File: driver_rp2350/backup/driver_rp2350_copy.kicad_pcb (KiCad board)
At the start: 6 copper layers, 45 x 45 mm, 463 parts, among them J1 Conn_01x04, J2 Conn_01x05, J3 Conn_01x05, J4 Conn_01x05, J5 Conn_01x05, SW1 SW_Push, SW2 SW_Push, U1 APS6404L-3SQR, U10 UCC27517, U11 UCC27517, U12 UCC27517, U13 UCC27517, U14 UCC27517, U15 UCC27517, U16 UCC27517, U17 UCC27517, U18 UCC27517, U19 UCC27517, U2 RP2354B_80QFN, U20 UCC27517, U21 UCC27517, U22 UCC27517, U23 UCC27517, U24 UCC27517, U25 UCC27517, U26 UCC27517, U27 UCC27517, U28 UCC27517, U29 UCC27517, U3 UCC27517, U30 UCC27517, U31 UCC27517, U32 UCC27517, U33 UCC27517, U34 UCC27517, U35 UCC27517, U36 UCC27517, U37 UCC27517, U38 UCC27517, U39 AP2112K-3.3, U4 UCC27517, U5 UCC27517, U6 UCC27517, U7 UCC27517, U8 UCC27517, U9 UCC27517, Y1 ABM8-272-T3

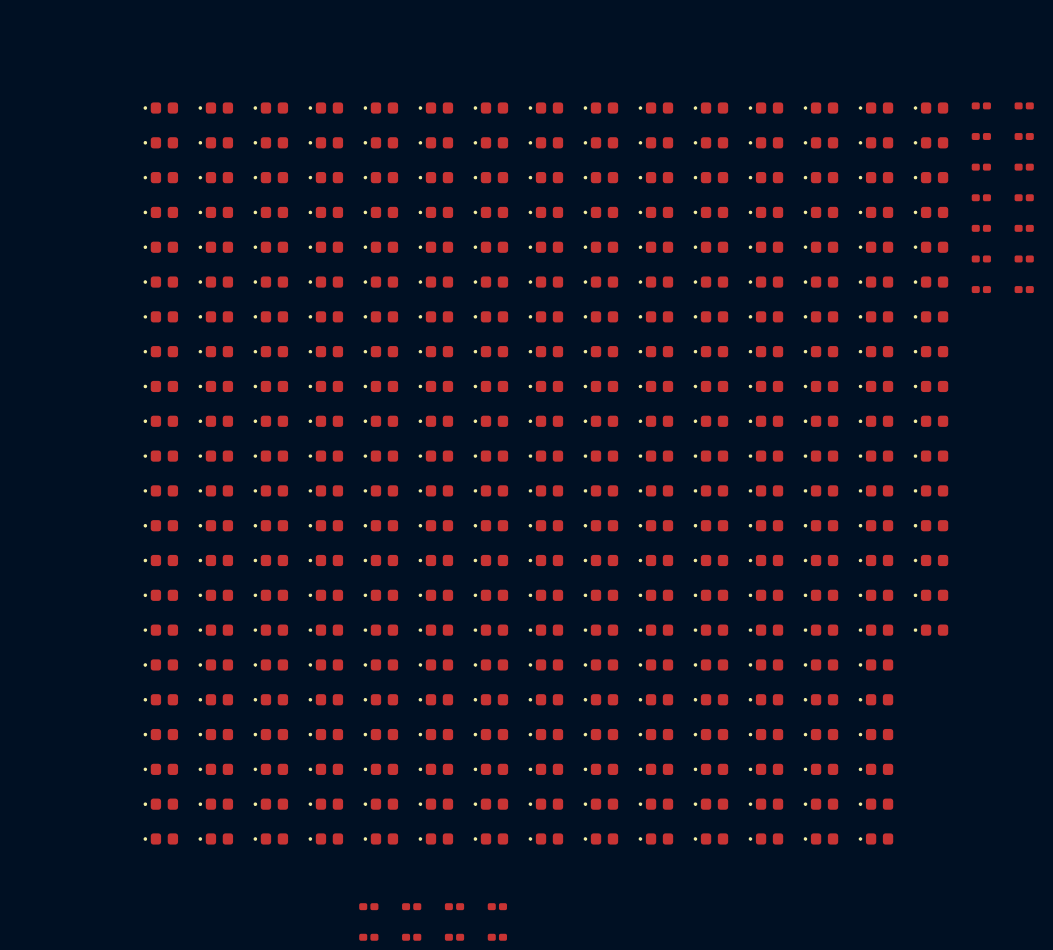
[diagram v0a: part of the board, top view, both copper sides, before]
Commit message: Worked on multi-color led layout.
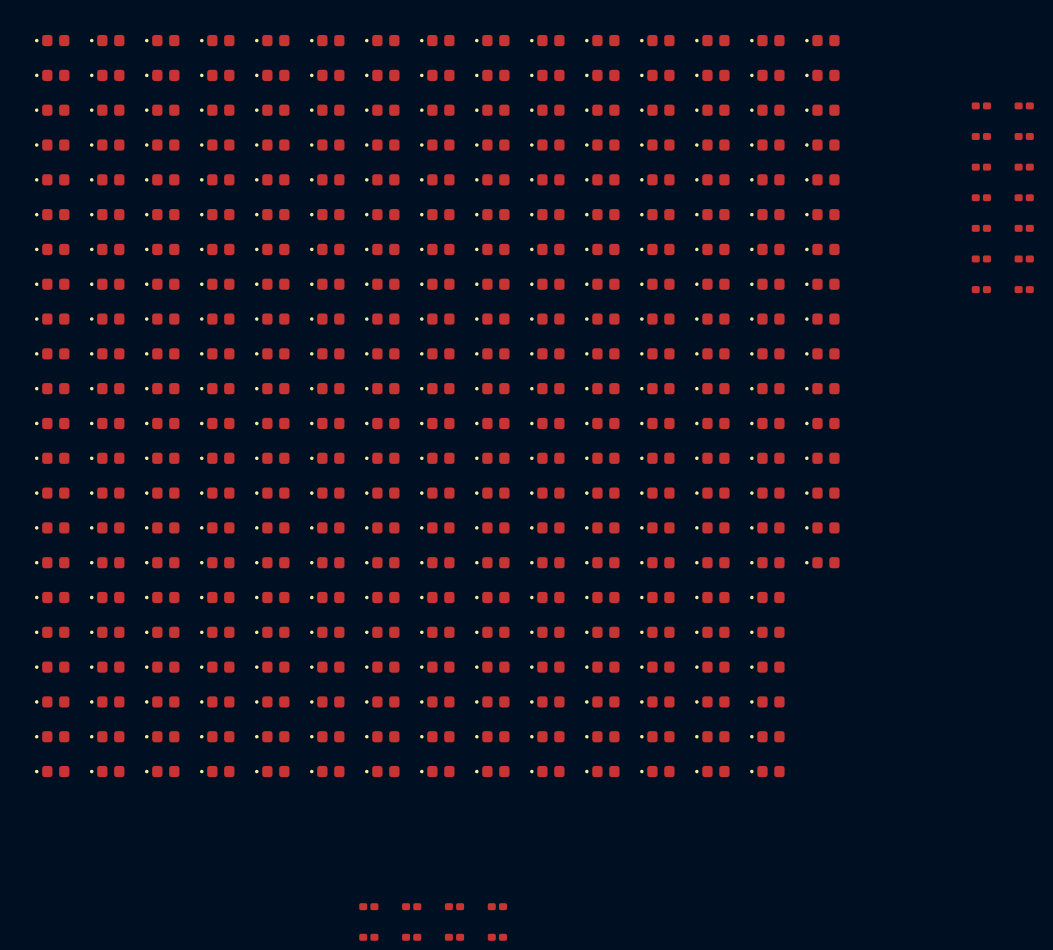
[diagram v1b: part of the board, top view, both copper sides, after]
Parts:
- removed D_0A1, D_0B1, D_0C1, D_0D1, D_0E1, D_0F1, D_0G1, D_0H1, D_1, D_10, D_100, D_11, D_12, D_13, D_14, D_15, D_16, D_17, D_18, D_19, D_1A1, D_1B1, D_1C1, D_1D1, D_1E1, D_1F1, D_1G1, D_1H1, D_2, D_20, D_21, D_22, D_23, D_24, D_25, D_26, D_27, D_28, D_29, D_2A1, D_2B1, D_2C1, D_2D1, D_2E1, D_2F1, D_2G1, D_2H1, D_3, D_30, D_31, D_32, D_33, D_34, D_35, D_36, D_37, D_38, D_39, D_3A1, D_3B1, D_3C1, D_3D1, D_3E1, D_3F1, D_3G1, D_3H1, D_4, D_40, D_41, D_42, D_43, D_44, D_45, D_46, D_47, D_48, D_49, D_4A1, D_4B1, D_4C1, D_4D1, D_4E1, D_4F1, D_4G1, D_4H1, D_5, D_50, D_51, D_52, D_53, D_54, D_55, D_56, D_57, D_58, D_59, D_5A1, D_5B1, D_5C1, D_5D1, D_5E1, D_5F1, D_5G1, D_5H1, D_6, D_60, D_61, D_62, D_63, D_64, D_65, D_66, D_67, D_68, D_69, D_6A1, D_6B1, D_6C1, D_6D1, D_6E1, D_6F1, D_6G1, D_6H1, D_7, D_70, D_71, D_72, D_73, D_74, D_75, D_76, D_77, D_78, D_79, D_7A1, D_7B1, D_7C1, D_7D1, D_7E1, D_7F1, D_7G1, D_7H1, D_8, D_80, D_81, D_82, D_83, D_84, D_85, D_86, D_87, D_88, D_89, D_8A1, D_8B1, D_8C1, D_8D1, D_8E1, D_8F1, D_8G1, D_8H1, D_9, D_90, D_91, D_92, D_93, D_94, D_95, D_96, D_97, D_98, D_99, D_9A1, D_9B1, D_9C1, D_9D1, D_9E1, D_9F1, D_9G1, D_9H1, D_A1, D_A10, D_A2, D_A3, D_A4, D_A5, D_A6, D_A7, D_A8, D_A9, D_AA1, D_AB1, D_AC1, D_AD1, D_AE1, D_AF1, D_AG1, D_AH1, D_B1, D_B10, D_B2, D_B3, D_B4, D_B5, D_B6, D_B7, D_B8, D_B9, D_BA1, D_BB1, D_BC1, D_BD1, D_BE1, D_BF1, D_BG1, D_BH1, D_C1, D_C10, D_C2, D_C3, D_C4, D_C5, D_C6, D_C7, D_C8, D_C9, D_CA1, D_CB1, D_CC1, D_CD1, D_CE1, D_CF1, D_CG1, D_CH1, D_D1, D_D10, D_D2, D_D3, D_D4, D_D5, D_D6, D_D7, D_D8, D_D9, D_DA1, D_DB1, D_DC1, D_DD1, D_DE1, D_DF1, D_DG1, D_DH1, D_E1, D_E10, D_E2, D_E3, D_E4, D_E5, D_E6, D_E7, D_E8, D_E9, D_EA1, D_EB1, D_EC1, D_ED1, D_EE1, D_EF1, D_EG1, D_EH1, D_F1, D_F10, D_F2, D_F3, D_F4, D_F5, D_F6, D_F7, D_F8, D_F9, D_FA1, D_FB1, D_FC1, D_FD1, D_FE1, D_FF1, D_FG1, D_FH1, D_G1, D_G10, D_G2, D_G3, D_G4, D_G5, D_G6, D_G7, D_G8, D_G9, D_GA1, D_GB1, D_GC1, D_GD1, D_GE1, D_GF1, D_GG1, D_GH1, D_H1, D_H10, D_H2, D_H3, D_H4, D_H5, D_H6, D_H7, D_H8, D_H9, D_HA1, D_HB1, D_HC1, D_HD1, D_HE1, D_HF1, D_HG1, D_HH1: LED, panel_custom:LED_0402_1005Metric
- added D1: LED, panel_custom:LED_0402_1005Metric, F.Cu at (-66.4, -11.2)
- added D10: LED, panel_custom:LED_0402_1005Metric, F.Cu at (-66.4, 6.72)
- added D100: LED, panel_custom:LED_0402_1005Metric, F.Cu at (-53.8, 10.7)
- added D101: LED, panel_custom:LED_0402_1005Metric, F.Cu at (-53.8, 12.7)
- added D102: LED, panel_custom:LED_0402_1005Metric, F.Cu at (-53.8, 14.7)
- added D103: LED, panel_custom:LED_0402_1005Metric, F.Cu at (-53.8, 16.7)
- added D104: LED, panel_custom:LED_0402_1005Metric, F.Cu at (-53.8, 18.7)
- added D105: LED, panel_custom:LED_0402_1005Metric, F.Cu at (-53.8, 20.6)
- added D106: LED, panel_custom:LED_0402_1005Metric, F.Cu at (-53.8, 22.6)
- added D107: LED, panel_custom:LED_0402_1005Metric, F.Cu at (-53.8, 24.6)
- added D108: LED, panel_custom:LED_0402_1005Metric, F.Cu at (-53.8, 26.6)
- added D109: LED, panel_custom:LED_0402_1005Metric, F.Cu at (-53.8, 28.6)
- added D11: LED, panel_custom:LED_0402_1005Metric, F.Cu at (-66.4, 8.71)
- added D110: LED, panel_custom:LED_0402_1005Metric, F.Cu at (-53.8, 30.6)
- added D111: LED, panel_custom:LED_0402_1005Metric, F.Cu at (-50.6, -11.2)
- added D112: LED, panel_custom:LED_0402_1005Metric, F.Cu at (-50.6, -9.20)
- added D113: LED, panel_custom:LED_0402_1005Metric, F.Cu at (-50.6, -7.21)
- added D114: LED, panel_custom:LED_0402_1005Metric, F.Cu at (-50.6, -5.22)
- added D115: LED, panel_custom:LED_0402_1005Metric, F.Cu at (-50.6, -3.23)
- added D116: LED, panel_custom:LED_0402_1005Metric, F.Cu at (-50.6, -1.24)
- added D117: LED, panel_custom:LED_0402_1005Metric, F.Cu at (-50.6, 0.75)
- added D118: LED, panel_custom:LED_0402_1005Metric, F.Cu at (-50.6, 2.74)
- added D119: LED, panel_custom:LED_0402_1005Metric, F.Cu at (-50.6, 4.73)
- added D12: LED, panel_custom:LED_0402_1005Metric, F.Cu at (-66.4, 10.7)
- added D120: LED, panel_custom:LED_0402_1005Metric, F.Cu at (-50.6, 6.72)
- added D121: LED, panel_custom:LED_0402_1005Metric, F.Cu at (-50.6, 8.71)
- added D122: LED, panel_custom:LED_0402_1005Metric, F.Cu at (-50.6, 10.7)
- added D123: LED, panel_custom:LED_0402_1005Metric, F.Cu at (-50.6, 12.7)
- added D124: LED, panel_custom:LED_0402_1005Metric, F.Cu at (-50.6, 14.7)
- added D125: LED, panel_custom:LED_0402_1005Metric, F.Cu at (-50.6, 16.7)
- added D126: LED, panel_custom:LED_0402_1005Metric, F.Cu at (-50.6, 18.7)
- added D127: LED, panel_custom:LED_0402_1005Metric, F.Cu at (-50.6, 20.6)
- added D128: LED, panel_custom:LED_0402_1005Metric, F.Cu at (-50.6, 22.6)
- added D129: LED, panel_custom:LED_0402_1005Metric, F.Cu at (-50.6, 24.6)
- added D13: LED, panel_custom:LED_0402_1005Metric, F.Cu at (-66.4, 12.7)
- added D130: LED, panel_custom:LED_0402_1005Metric, F.Cu at (-50.6, 26.6)
- added D131: LED, panel_custom:LED_0402_1005Metric, F.Cu at (-50.6, 28.6)
- added D132: LED, panel_custom:LED_0402_1005Metric, F.Cu at (-50.6, 30.6)
- added D133: LED, panel_custom:LED_0402_1005Metric, F.Cu at (-47.5, -11.2)
- added D134: LED, panel_custom:LED_0402_1005Metric, F.Cu at (-47.5, -9.20)
- added D135: LED, panel_custom:LED_0402_1005Metric, F.Cu at (-47.5, -7.21)
- added D136: LED, panel_custom:LED_0402_1005Metric, F.Cu at (-47.5, -5.22)
- added D137: LED, panel_custom:LED_0402_1005Metric, F.Cu at (-47.5, -3.23)
- added D138: LED, panel_custom:LED_0402_1005Metric, F.Cu at (-47.5, -1.24)
- added D139: LED, panel_custom:LED_0402_1005Metric, F.Cu at (-47.5, 0.75)
- added D14: LED, panel_custom:LED_0402_1005Metric, F.Cu at (-66.4, 14.7)
- added D140: LED, panel_custom:LED_0402_1005Metric, F.Cu at (-47.5, 2.74)
- added D141: LED, panel_custom:LED_0402_1005Metric, F.Cu at (-47.5, 4.73)
- added D142: LED, panel_custom:LED_0402_1005Metric, F.Cu at (-47.5, 6.72)
- added D143: LED, panel_custom:LED_0402_1005Metric, F.Cu at (-47.5, 8.71)
- added D144: LED, panel_custom:LED_0402_1005Metric, F.Cu at (-47.5, 10.7)
- added D145: LED, panel_custom:LED_0402_1005Metric, F.Cu at (-47.5, 12.7)
- added D146: LED, panel_custom:LED_0402_1005Metric, F.Cu at (-47.5, 14.7)
- added D147: LED, panel_custom:LED_0402_1005Metric, F.Cu at (-47.5, 16.7)
- added D148: LED, panel_custom:LED_0402_1005Metric, F.Cu at (-47.5, 18.7)
- added D149: LED, panel_custom:LED_0402_1005Metric, F.Cu at (-47.5, 20.6)
- added D15: LED, panel_custom:LED_0402_1005Metric, F.Cu at (-66.4, 16.7)
- added D150: LED, panel_custom:LED_0402_1005Metric, F.Cu at (-47.5, 22.6)
- added D151: LED, panel_custom:LED_0402_1005Metric, F.Cu at (-47.5, 24.6)
- added D152: LED, panel_custom:LED_0402_1005Metric, F.Cu at (-47.5, 26.6)
- added D153: LED, panel_custom:LED_0402_1005Metric, F.Cu at (-47.5, 28.6)
- added D154: LED, panel_custom:LED_0402_1005Metric, F.Cu at (-47.5, 30.6)
- added D155: LED, panel_custom:LED_0402_1005Metric, F.Cu at (-44.4, -11.2)
- added D156: LED, panel_custom:LED_0402_1005Metric, F.Cu at (-44.4, -9.20)
- added D157: LED, panel_custom:LED_0402_1005Metric, F.Cu at (-44.4, -7.21)
- added D158: LED, panel_custom:LED_0402_1005Metric, F.Cu at (-44.4, -5.22)
- added D159: LED, panel_custom:LED_0402_1005Metric, F.Cu at (-44.4, -3.23)
- added D16: LED, panel_custom:LED_0402_1005Metric, F.Cu at (-66.4, 18.7)
- added D160: LED, panel_custom:LED_0402_1005Metric, F.Cu at (-44.4, -1.24)
- added D161: LED, panel_custom:LED_0402_1005Metric, F.Cu at (-44.4, 0.75)
- added D162: LED, panel_custom:LED_0402_1005Metric, F.Cu at (-44.4, 2.74)
- added D163: LED, panel_custom:LED_0402_1005Metric, F.Cu at (-44.4, 4.73)
- added D164: LED, panel_custom:LED_0402_1005Metric, F.Cu at (-44.4, 6.72)
- added D165: LED, panel_custom:LED_0402_1005Metric, F.Cu at (-44.4, 8.71)
- added D166: LED, panel_custom:LED_0402_1005Metric, F.Cu at (-44.4, 10.7)
- added D167: LED, panel_custom:LED_0402_1005Metric, F.Cu at (-44.4, 12.7)
- added D168: LED, panel_custom:LED_0402_1005Metric, F.Cu at (-44.4, 14.7)
- added D169: LED, panel_custom:LED_0402_1005Metric, F.Cu at (-44.4, 16.7)
- added D17: LED, panel_custom:LED_0402_1005Metric, F.Cu at (-66.4, 20.6)
- added D170: LED, panel_custom:LED_0402_1005Metric, F.Cu at (-44.4, 18.7)
- added D171: LED, panel_custom:LED_0402_1005Metric, F.Cu at (-44.4, 20.6)
- added D172: LED, panel_custom:LED_0402_1005Metric, F.Cu at (-44.4, 22.6)
- added D173: LED, panel_custom:LED_0402_1005Metric, F.Cu at (-44.4, 24.6)
- added D174: LED, panel_custom:LED_0402_1005Metric, F.Cu at (-44.4, 26.6)
- added D175: LED, panel_custom:LED_0402_1005Metric, F.Cu at (-44.4, 28.6)
- added D176: LED, panel_custom:LED_0402_1005Metric, F.Cu at (-44.4, 30.6)
- added D177: LED, panel_custom:LED_0402_1005Metric, F.Cu at (-41.2, -11.2)
- added D178: LED, panel_custom:LED_0402_1005Metric, F.Cu at (-41.2, -9.20)
- added D179: LED, panel_custom:LED_0402_1005Metric, F.Cu at (-41.2, -7.21)
- added D18: LED, panel_custom:LED_0402_1005Metric, F.Cu at (-66.4, 22.6)
- added D180: LED, panel_custom:LED_0402_1005Metric, F.Cu at (-41.2, -5.22)
- added D181: LED, panel_custom:LED_0402_1005Metric, F.Cu at (-41.2, -3.23)
- added D182: LED, panel_custom:LED_0402_1005Metric, F.Cu at (-41.2, -1.24)
- added D183: LED, panel_custom:LED_0402_1005Metric, F.Cu at (-41.2, 0.75)
- added D184: LED, panel_custom:LED_0402_1005Metric, F.Cu at (-41.2, 2.74)
- added D185: LED, panel_custom:LED_0402_1005Metric, F.Cu at (-41.2, 4.73)
- added D186: LED, panel_custom:LED_0402_1005Metric, F.Cu at (-41.2, 6.72)
- added D187: LED, panel_custom:LED_0402_1005Metric, F.Cu at (-41.2, 8.71)
- added D188: LED, panel_custom:LED_0402_1005Metric, F.Cu at (-41.2, 10.7)
- added D189: LED, panel_custom:LED_0402_1005Metric, F.Cu at (-41.2, 12.7)
- added D19: LED, panel_custom:LED_0402_1005Metric, F.Cu at (-66.4, 24.6)
- added D190: LED, panel_custom:LED_0402_1005Metric, F.Cu at (-41.2, 14.7)
- added D191: LED, panel_custom:LED_0402_1005Metric, F.Cu at (-41.2, 16.7)
- added D192: LED, panel_custom:LED_0402_1005Metric, F.Cu at (-41.2, 18.7)
- added D193: LED, panel_custom:LED_0402_1005Metric, F.Cu at (-41.2, 20.6)
- added D194: LED, panel_custom:LED_0402_1005Metric, F.Cu at (-41.2, 22.6)
- added D195: LED, panel_custom:LED_0402_1005Metric, F.Cu at (-41.2, 24.6)
- added D196: LED, panel_custom:LED_0402_1005Metric, F.Cu at (-41.2, 26.6)
- added D197: LED, panel_custom:LED_0402_1005Metric, F.Cu at (-41.2, 28.6)
- added D198: LED, panel_custom:LED_0402_1005Metric, F.Cu at (-41.2, 30.6)
- added D199: LED, panel_custom:LED_0402_1005Metric, F.Cu at (-38.1, -11.2)
- added D2: LED, panel_custom:LED_0402_1005Metric, F.Cu at (-66.4, -9.20)
- added D20: LED, panel_custom:LED_0402_1005Metric, F.Cu at (-66.4, 26.6)
- added D200: LED, panel_custom:LED_0402_1005Metric, F.Cu at (-38.1, -9.20)
- added D201: LED, panel_custom:LED_0402_1005Metric, F.Cu at (-38.1, -7.21)
- added D202: LED, panel_custom:LED_0402_1005Metric, F.Cu at (-38.1, -5.22)
- added D203: LED, panel_custom:LED_0402_1005Metric, F.Cu at (-38.1, -3.23)
- added D204: LED, panel_custom:LED_0402_1005Metric, F.Cu at (-38.1, -1.24)
- added D205: LED, panel_custom:LED_0402_1005Metric, F.Cu at (-38.1, 0.75)
- added D206: LED, panel_custom:LED_0402_1005Metric, F.Cu at (-38.1, 2.74)
- added D207: LED, panel_custom:LED_0402_1005Metric, F.Cu at (-38.1, 4.73)
- added D208: LED, panel_custom:LED_0402_1005Metric, F.Cu at (-38.1, 6.72)
- added D209: LED, panel_custom:LED_0402_1005Metric, F.Cu at (-38.1, 8.71)
- added D21: LED, panel_custom:LED_0402_1005Metric, F.Cu at (-66.4, 28.6)
- added D210: LED, panel_custom:LED_0402_1005Metric, F.Cu at (-38.1, 10.7)
- added D211: LED, panel_custom:LED_0402_1005Metric, F.Cu at (-38.1, 12.7)
- added D212: LED, panel_custom:LED_0402_1005Metric, F.Cu at (-38.1, 14.7)
- added D213: LED, panel_custom:LED_0402_1005Metric, F.Cu at (-38.1, 16.7)
- added D214: LED, panel_custom:LED_0402_1005Metric, F.Cu at (-38.1, 18.7)
- added D215: LED, panel_custom:LED_0402_1005Metric, F.Cu at (-38.1, 20.6)
- added D216: LED, panel_custom:LED_0402_1005Metric, F.Cu at (-38.1, 22.6)
- added D217: LED, panel_custom:LED_0402_1005Metric, F.Cu at (-38.1, 24.6)
- added D218: LED, panel_custom:LED_0402_1005Metric, F.Cu at (-38.1, 26.6)
- added D219: LED, panel_custom:LED_0402_1005Metric, F.Cu at (-38.1, 28.6)
- added D22: LED, panel_custom:LED_0402_1005Metric, F.Cu at (-66.4, 30.6)
- added D220: LED, panel_custom:LED_0402_1005Metric, F.Cu at (-38.1, 30.6)
- added D221: LED, panel_custom:LED_0402_1005Metric, F.Cu at (-34.9, -11.2)
- added D222: LED, panel_custom:LED_0402_1005Metric, F.Cu at (-34.9, -9.20)
- added D223: LED, panel_custom:LED_0402_1005Metric, F.Cu at (-34.9, -7.21)
- added D224: LED, panel_custom:LED_0402_1005Metric, F.Cu at (-34.9, -5.22)
- added D225: LED, panel_custom:LED_0402_1005Metric, F.Cu at (-34.9, -3.23)
- added D226: LED, panel_custom:LED_0402_1005Metric, F.Cu at (-34.9, -1.24)
- added D227: LED, panel_custom:LED_0402_1005Metric, F.Cu at (-34.9, 0.75)
- added D228: LED, panel_custom:LED_0402_1005Metric, F.Cu at (-34.9, 2.74)
- added D229: LED, panel_custom:LED_0402_1005Metric, F.Cu at (-34.9, 4.73)
- added D23: LED, panel_custom:LED_0402_1005Metric, F.Cu at (-63.2, -11.2)
- added D230: LED, panel_custom:LED_0402_1005Metric, F.Cu at (-34.9, 6.72)
- added D231: LED, panel_custom:LED_0402_1005Metric, F.Cu at (-34.9, 8.71)
- added D232: LED, panel_custom:LED_0402_1005Metric, F.Cu at (-34.9, 10.7)
- added D233: LED, panel_custom:LED_0402_1005Metric, F.Cu at (-34.9, 12.7)
- added D234: LED, panel_custom:LED_0402_1005Metric, F.Cu at (-34.9, 14.7)
- added D235: LED, panel_custom:LED_0402_1005Metric, F.Cu at (-34.9, 16.7)
- added D236: LED, panel_custom:LED_0402_1005Metric, F.Cu at (-34.9, 18.7)
- added D237: LED, panel_custom:LED_0402_1005Metric, F.Cu at (-34.9, 20.6)
- added D238: LED, panel_custom:LED_0402_1005Metric, F.Cu at (-34.9, 22.6)
- added D239: LED, panel_custom:LED_0402_1005Metric, F.Cu at (-34.9, 24.6)
- added D24: LED, panel_custom:LED_0402_1005Metric, F.Cu at (-63.2, -9.20)
- added D240: LED, panel_custom:LED_0402_1005Metric, F.Cu at (-34.9, 26.6)
- added D241: LED, panel_custom:LED_0402_1005Metric, F.Cu at (-34.9, 28.6)
- added D242: LED, panel_custom:LED_0402_1005Metric, F.Cu at (-34.9, 30.6)
- added D243: LED, panel_custom:LED_0402_1005Metric, F.Cu at (-31.8, -11.2)
- added D244: LED, panel_custom:LED_0402_1005Metric, F.Cu at (-31.8, -9.20)
- added D245: LED, panel_custom:LED_0402_1005Metric, F.Cu at (-31.8, -7.21)
- added D246: LED, panel_custom:LED_0402_1005Metric, F.Cu at (-31.8, -5.22)
- added D247: LED, panel_custom:LED_0402_1005Metric, F.Cu at (-31.8, -3.23)
- added D248: LED, panel_custom:LED_0402_1005Metric, F.Cu at (-31.8, -1.24)
- added D249: LED, panel_custom:LED_0402_1005Metric, F.Cu at (-31.8, 0.75)
- added D25: LED, panel_custom:LED_0402_1005Metric, F.Cu at (-63.2, -7.21)
- added D250: LED, panel_custom:LED_0402_1005Metric, F.Cu at (-31.8, 2.74)
- added D251: LED, panel_custom:LED_0402_1005Metric, F.Cu at (-31.8, 4.73)
- added D252: LED, panel_custom:LED_0402_1005Metric, F.Cu at (-31.8, 6.72)
- added D253: LED, panel_custom:LED_0402_1005Metric, F.Cu at (-31.8, 8.71)
- added D254: LED, panel_custom:LED_0402_1005Metric, F.Cu at (-31.8, 10.7)
- added D255: LED, panel_custom:LED_0402_1005Metric, F.Cu at (-31.8, 12.7)
- added D256: LED, panel_custom:LED_0402_1005Metric, F.Cu at (-31.8, 14.7)
- added D257: LED, panel_custom:LED_0402_1005Metric, F.Cu at (-31.8, 16.7)
- added D258: LED, panel_custom:LED_0402_1005Metric, F.Cu at (-31.8, 18.7)
- added D259: LED, panel_custom:LED_0402_1005Metric, F.Cu at (-31.8, 20.6)
- added D26: LED, panel_custom:LED_0402_1005Metric, F.Cu at (-63.2, -5.22)
- added D260: LED, panel_custom:LED_0402_1005Metric, F.Cu at (-31.8, 22.6)
- added D261: LED, panel_custom:LED_0402_1005Metric, F.Cu at (-31.8, 24.6)
- added D262: LED, panel_custom:LED_0402_1005Metric, F.Cu at (-31.8, 26.6)
- added D263: LED, panel_custom:LED_0402_1005Metric, F.Cu at (-31.8, 28.6)
- added D264: LED, panel_custom:LED_0402_1005Metric, F.Cu at (-31.8, 30.6)
- added D265: LED, panel_custom:LED_0402_1005Metric, F.Cu at (-28.6, -11.2)
- added D266: LED, panel_custom:LED_0402_1005Metric, F.Cu at (-28.6, -9.20)
- added D267: LED, panel_custom:LED_0402_1005Metric, F.Cu at (-28.6, -7.21)
- added D268: LED, panel_custom:LED_0402_1005Metric, F.Cu at (-28.6, -5.22)
- added D269: LED, panel_custom:LED_0402_1005Metric, F.Cu at (-28.6, -3.23)
- added D27: LED, panel_custom:LED_0402_1005Metric, F.Cu at (-63.2, -3.23)
- added D270: LED, panel_custom:LED_0402_1005Metric, F.Cu at (-28.6, -1.24)
- added D271: LED, panel_custom:LED_0402_1005Metric, F.Cu at (-28.6, 0.75)
- added D272: LED, panel_custom:LED_0402_1005Metric, F.Cu at (-28.6, 2.74)
- added D273: LED, panel_custom:LED_0402_1005Metric, F.Cu at (-28.6, 4.73)
- added D274: LED, panel_custom:LED_0402_1005Metric, F.Cu at (-28.6, 6.72)
- added D275: LED, panel_custom:LED_0402_1005Metric, F.Cu at (-28.6, 8.71)
- added D276: LED, panel_custom:LED_0402_1005Metric, F.Cu at (-28.6, 10.7)
- added D277: LED, panel_custom:LED_0402_1005Metric, F.Cu at (-28.6, 12.7)
- added D278: LED, panel_custom:LED_0402_1005Metric, F.Cu at (-28.6, 14.7)
- added D279: LED, panel_custom:LED_0402_1005Metric, F.Cu at (-28.6, 16.7)
- added D28: LED, panel_custom:LED_0402_1005Metric, F.Cu at (-63.2, -1.24)
- added D280: LED, panel_custom:LED_0402_1005Metric, F.Cu at (-28.6, 18.7)
- added D281: LED, panel_custom:LED_0402_1005Metric, F.Cu at (-28.6, 20.6)
- added D282: LED, panel_custom:LED_0402_1005Metric, F.Cu at (-28.6, 22.6)
- added D283: LED, panel_custom:LED_0402_1005Metric, F.Cu at (-28.6, 24.6)
- added D284: LED, panel_custom:LED_0402_1005Metric, F.Cu at (-28.6, 26.6)
- added D285: LED, panel_custom:LED_0402_1005Metric, F.Cu at (-28.6, 28.6)
- added D286: LED, panel_custom:LED_0402_1005Metric, F.Cu at (-28.6, 30.6)
- added D287: LED, panel_custom:LED_0402_1005Metric, F.Cu at (-25.5, -11.2)
- added D288: LED, panel_custom:LED_0402_1005Metric, F.Cu at (-25.5, -9.20)
- added D289: LED, panel_custom:LED_0402_1005Metric, F.Cu at (-25.5, -7.21)
- added D29: LED, panel_custom:LED_0402_1005Metric, F.Cu at (-63.2, 0.75)
- added D290: LED, panel_custom:LED_0402_1005Metric, F.Cu at (-25.5, -5.22)
- added D291: LED, panel_custom:LED_0402_1005Metric, F.Cu at (-25.5, -3.23)
- added D292: LED, panel_custom:LED_0402_1005Metric, F.Cu at (-25.5, -1.24)
- added D293: LED, panel_custom:LED_0402_1005Metric, F.Cu at (-25.5, 0.75)
- added D294: LED, panel_custom:LED_0402_1005Metric, F.Cu at (-25.5, 2.74)
- added D295: LED, panel_custom:LED_0402_1005Metric, F.Cu at (-25.5, 4.73)
- added D296: LED, panel_custom:LED_0402_1005Metric, F.Cu at (-25.5, 6.72)
- added D297: LED, panel_custom:LED_0402_1005Metric, F.Cu at (-25.5, 8.71)
- added D298: LED, panel_custom:LED_0402_1005Metric, F.Cu at (-25.5, 10.7)
- added D299: LED, panel_custom:LED_0402_1005Metric, F.Cu at (-25.5, 12.7)
- added D3: LED, panel_custom:LED_0402_1005Metric, F.Cu at (-66.4, -7.21)
- added D30: LED, panel_custom:LED_0402_1005Metric, F.Cu at (-63.2, 2.74)
- added D300: LED, panel_custom:LED_0402_1005Metric, F.Cu at (-25.5, 14.7)
- added D301: LED, panel_custom:LED_0402_1005Metric, F.Cu at (-25.5, 16.7)
- added D302: LED, panel_custom:LED_0402_1005Metric, F.Cu at (-25.5, 18.7)
- added D303: LED, panel_custom:LED_0402_1005Metric, F.Cu at (-25.5, 20.6)
- added D304: LED, panel_custom:LED_0402_1005Metric, F.Cu at (-25.5, 22.6)
- added D305: LED, panel_custom:LED_0402_1005Metric, F.Cu at (-25.5, 24.6)
- added D306: LED, panel_custom:LED_0402_1005Metric, F.Cu at (-25.5, 26.6)
- added D307: LED, panel_custom:LED_0402_1005Metric, F.Cu at (-25.5, 28.6)
- added D308: LED, panel_custom:LED_0402_1005Metric, F.Cu at (-25.5, 30.6)
- added D309: LED, panel_custom:LED_0402_1005Metric, F.Cu at (-22.3, -11.2)
- added D31: LED, panel_custom:LED_0402_1005Metric, F.Cu at (-63.2, 4.73)
- added D310: LED, panel_custom:LED_0402_1005Metric, F.Cu at (-22.3, -9.20)
- added D311: LED, panel_custom:LED_0402_1005Metric, F.Cu at (-22.3, -7.21)
- added D312: LED, panel_custom:LED_0402_1005Metric, F.Cu at (-22.3, -5.22)
- added D313: LED, panel_custom:LED_0402_1005Metric, F.Cu at (-22.3, -3.23)
- added D314: LED, panel_custom:LED_0402_1005Metric, F.Cu at (-22.3, -1.24)
- added D315: LED, panel_custom:LED_0402_1005Metric, F.Cu at (-22.3, 0.75)
- added D316: LED, panel_custom:LED_0402_1005Metric, F.Cu at (-22.3, 2.74)
- added D317: LED, panel_custom:LED_0402_1005Metric, F.Cu at (-22.3, 4.73)
- added D318: LED, panel_custom:LED_0402_1005Metric, F.Cu at (-22.3, 6.72)
- added D319: LED, panel_custom:LED_0402_1005Metric, F.Cu at (-22.3, 8.71)
- added D32: LED, panel_custom:LED_0402_1005Metric, F.Cu at (-63.2, 6.72)
- added D320: LED, panel_custom:LED_0402_1005Metric, F.Cu at (-22.3, 10.7)
- added D321: LED, panel_custom:LED_0402_1005Metric, F.Cu at (-22.3, 12.7)
- added D322: LED, panel_custom:LED_0402_1005Metric, F.Cu at (-22.3, 14.7)
- added D323: LED, panel_custom:LED_0402_1005Metric, F.Cu at (-22.3, 16.7)
- added D324: LED, panel_custom:LED_0402_1005Metric, F.Cu at (-22.3, 18.7)
- added D33: LED, panel_custom:LED_0402_1005Metric, F.Cu at (-63.2, 8.71)
- added D34: LED, panel_custom:LED_0402_1005Metric, F.Cu at (-63.2, 10.7)
- added D35: LED, panel_custom:LED_0402_1005Metric, F.Cu at (-63.2, 12.7)
- added D36: LED, panel_custom:LED_0402_1005Metric, F.Cu at (-63.2, 14.7)
- added D37: LED, panel_custom:LED_0402_1005Metric, F.Cu at (-63.2, 16.7)
- added D38: LED, panel_custom:LED_0402_1005Metric, F.Cu at (-63.2, 18.7)
- added D39: LED, panel_custom:LED_0402_1005Metric, F.Cu at (-63.2, 20.6)
- added D4: LED, panel_custom:LED_0402_1005Metric, F.Cu at (-66.4, -5.22)
- added D40: LED, panel_custom:LED_0402_1005Metric, F.Cu at (-63.2, 22.6)
- added D41: LED, panel_custom:LED_0402_1005Metric, F.Cu at (-63.2, 24.6)
- added D42: LED, panel_custom:LED_0402_1005Metric, F.Cu at (-63.2, 26.6)
- added D43: LED, panel_custom:LED_0402_1005Metric, F.Cu at (-63.2, 28.6)
- added D44: LED, panel_custom:LED_0402_1005Metric, F.Cu at (-63.2, 30.6)
- added D45: LED, panel_custom:LED_0402_1005Metric, F.Cu at (-60.1, -11.2)
- added D46: LED, panel_custom:LED_0402_1005Metric, F.Cu at (-60.1, -9.20)
- added D47: LED, panel_custom:LED_0402_1005Metric, F.Cu at (-60.1, -7.21)
- added D48: LED, panel_custom:LED_0402_1005Metric, F.Cu at (-60.1, -5.22)
- added D49: LED, panel_custom:LED_0402_1005Metric, F.Cu at (-60.1, -3.23)
- added D5: LED, panel_custom:LED_0402_1005Metric, F.Cu at (-66.4, -3.23)
- added D50: LED, panel_custom:LED_0402_1005Metric, F.Cu at (-60.1, -1.24)
- added D51: LED, panel_custom:LED_0402_1005Metric, F.Cu at (-60.1, 0.75)
- added D52: LED, panel_custom:LED_0402_1005Metric, F.Cu at (-60.1, 2.74)
- added D53: LED, panel_custom:LED_0402_1005Metric, F.Cu at (-60.1, 4.73)
- added D54: LED, panel_custom:LED_0402_1005Metric, F.Cu at (-60.1, 6.72)
- added D55: LED, panel_custom:LED_0402_1005Metric, F.Cu at (-60.1, 8.71)
- added D56: LED, panel_custom:LED_0402_1005Metric, F.Cu at (-60.1, 10.7)
- added D57: LED, panel_custom:LED_0402_1005Metric, F.Cu at (-60.1, 12.7)
- added D58: LED, panel_custom:LED_0402_1005Metric, F.Cu at (-60.1, 14.7)
- added D59: LED, panel_custom:LED_0402_1005Metric, F.Cu at (-60.1, 16.7)
- added D6: LED, panel_custom:LED_0402_1005Metric, F.Cu at (-66.4, -1.24)
- added D60: LED, panel_custom:LED_0402_1005Metric, F.Cu at (-60.1, 18.7)
- added D61: LED, panel_custom:LED_0402_1005Metric, F.Cu at (-60.1, 20.6)
- added D62: LED, panel_custom:LED_0402_1005Metric, F.Cu at (-60.1, 22.6)
- added D63: LED, panel_custom:LED_0402_1005Metric, F.Cu at (-60.1, 24.6)
- added D64: LED, panel_custom:LED_0402_1005Metric, F.Cu at (-60.1, 26.6)
- added D65: LED, panel_custom:LED_0402_1005Metric, F.Cu at (-60.1, 28.6)
- added D66: LED, panel_custom:LED_0402_1005Metric, F.Cu at (-60.1, 30.6)
- added D67: LED, panel_custom:LED_0402_1005Metric, F.Cu at (-56.9, -11.2)
- added D68: LED, panel_custom:LED_0402_1005Metric, F.Cu at (-56.9, -9.20)
- added D69: LED, panel_custom:LED_0402_1005Metric, F.Cu at (-56.9, -7.21)
- added D7: LED, panel_custom:LED_0402_1005Metric, F.Cu at (-66.4, 0.75)
- added D70: LED, panel_custom:LED_0402_1005Metric, F.Cu at (-56.9, -5.22)
- added D71: LED, panel_custom:LED_0402_1005Metric, F.Cu at (-56.9, -3.23)
- added D72: LED, panel_custom:LED_0402_1005Metric, F.Cu at (-56.9, -1.24)
- added D73: LED, panel_custom:LED_0402_1005Metric, F.Cu at (-56.9, 0.75)
- added D74: LED, panel_custom:LED_0402_1005Metric, F.Cu at (-56.9, 2.74)
- added D75: LED, panel_custom:LED_0402_1005Metric, F.Cu at (-56.9, 4.73)
- added D76: LED, panel_custom:LED_0402_1005Metric, F.Cu at (-56.9, 6.72)
- added D77: LED, panel_custom:LED_0402_1005Metric, F.Cu at (-56.9, 8.71)
- added D78: LED, panel_custom:LED_0402_1005Metric, F.Cu at (-56.9, 10.7)
- added D79: LED, panel_custom:LED_0402_1005Metric, F.Cu at (-56.9, 12.7)
- added D8: LED, panel_custom:LED_0402_1005Metric, F.Cu at (-66.4, 2.74)
- added D80: LED, panel_custom:LED_0402_1005Metric, F.Cu at (-56.9, 14.7)
- added D81: LED, panel_custom:LED_0402_1005Metric, F.Cu at (-56.9, 16.7)
- added D82: LED, panel_custom:LED_0402_1005Metric, F.Cu at (-56.9, 18.7)
- added D83: LED, panel_custom:LED_0402_1005Metric, F.Cu at (-56.9, 20.6)
- added D84: LED, panel_custom:LED_0402_1005Metric, F.Cu at (-56.9, 22.6)
- added D85: LED, panel_custom:LED_0402_1005Metric, F.Cu at (-56.9, 24.6)
- added D86: LED, panel_custom:LED_0402_1005Metric, F.Cu at (-56.9, 26.6)
- added D87: LED, panel_custom:LED_0402_1005Metric, F.Cu at (-56.9, 28.6)
- added D88: LED, panel_custom:LED_0402_1005Metric, F.Cu at (-56.9, 30.6)
- added D89: LED, panel_custom:LED_0402_1005Metric, F.Cu at (-53.8, -11.2)
- added D9: LED, panel_custom:LED_0402_1005Metric, F.Cu at (-66.4, 4.73)
- added D90: LED, panel_custom:LED_0402_1005Metric, F.Cu at (-53.8, -9.20)
- added D91: LED, panel_custom:LED_0402_1005Metric, F.Cu at (-53.8, -7.21)
- added D92: LED, panel_custom:LED_0402_1005Metric, F.Cu at (-53.8, -5.22)
- added D93: LED, panel_custom:LED_0402_1005Metric, F.Cu at (-53.8, -3.23)
- added D94: LED, panel_custom:LED_0402_1005Metric, F.Cu at (-53.8, -1.24)
- added D95: LED, panel_custom:LED_0402_1005Metric, F.Cu at (-53.8, 0.75)
- added D96: LED, panel_custom:LED_0402_1005Metric, F.Cu at (-53.8, 2.74)
- added D97: LED, panel_custom:LED_0402_1005Metric, F.Cu at (-53.8, 4.73)
- added D98: LED, panel_custom:LED_0402_1005Metric, F.Cu at (-53.8, 6.72)
- added D99: LED, panel_custom:LED_0402_1005Metric, F.Cu at (-53.8, 8.71)
